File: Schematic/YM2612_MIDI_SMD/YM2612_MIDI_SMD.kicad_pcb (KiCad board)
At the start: 2 copper layers, 100 x 100 mm, 125 parts, among them J1 Barrel_Jack_12V, J2 USB_B, J3 DIN-5_180, J4 Audio-Jack-3, J5 Micro_SD_Card, J6 ICSP, SW1 SW_Push_Dual, SW10 SW_Push_Dual, SW2 SW_Push_Dual, SW3 SW_Push_Dual, SW4 SW_Push_Dual, SW5 SW_Push_Dual, SW6 SW_Push_Dual, SW7 SW_Push_Dual, SW8 SW_Push_Dual, SW9 Rotary_Encoder_Switch, U1 LM2596S-5, U10 LD1117S33TR_SOT223, U11 4050, U2 AT90USB1286-AU, U3 YM2612, U4 SN76489, U6 H11L1, U8 TPA3122D2, U9 TL062, Y1 16MHz

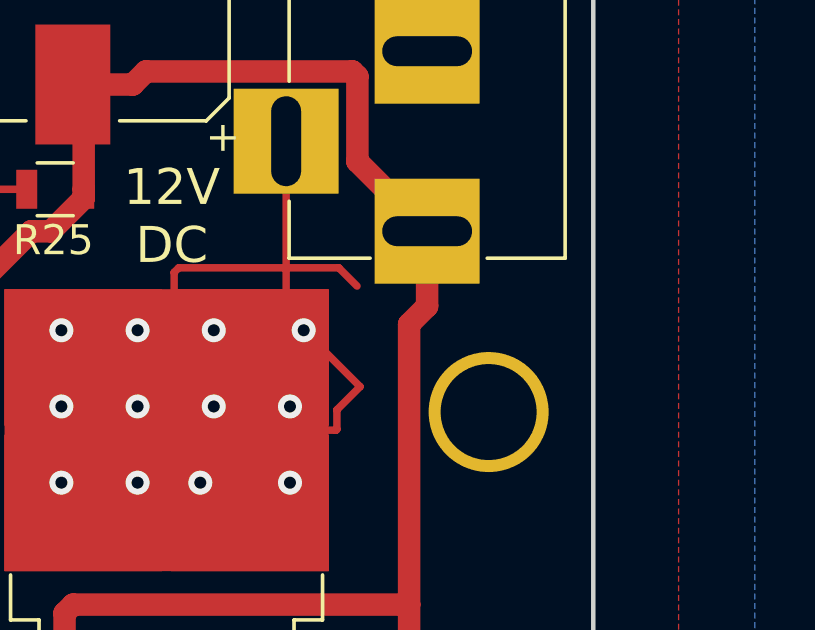
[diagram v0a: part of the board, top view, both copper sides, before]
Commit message: Added center-positive logo to FSS
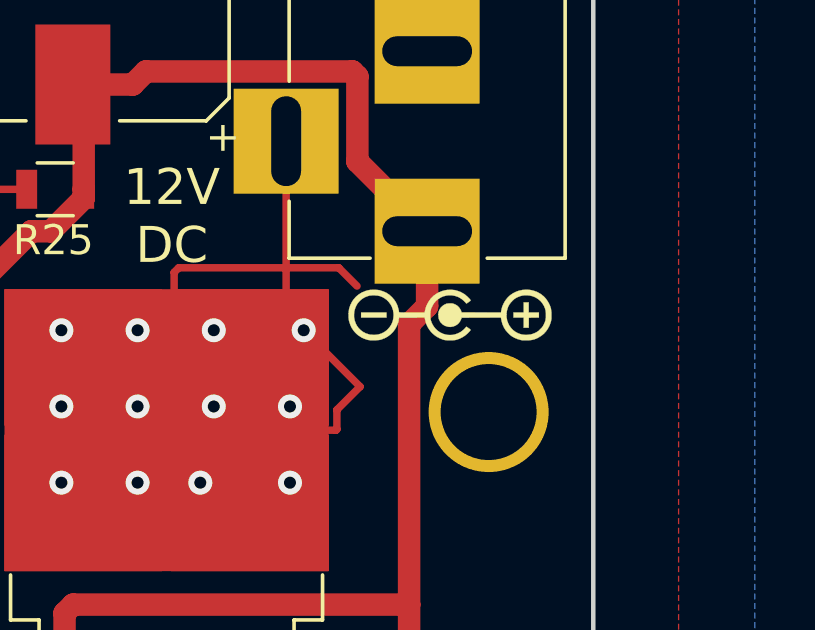
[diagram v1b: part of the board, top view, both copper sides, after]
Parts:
- added G***: LOGO, art:Center_Positive_Logo, F.Cu at (268.2, 63.0)

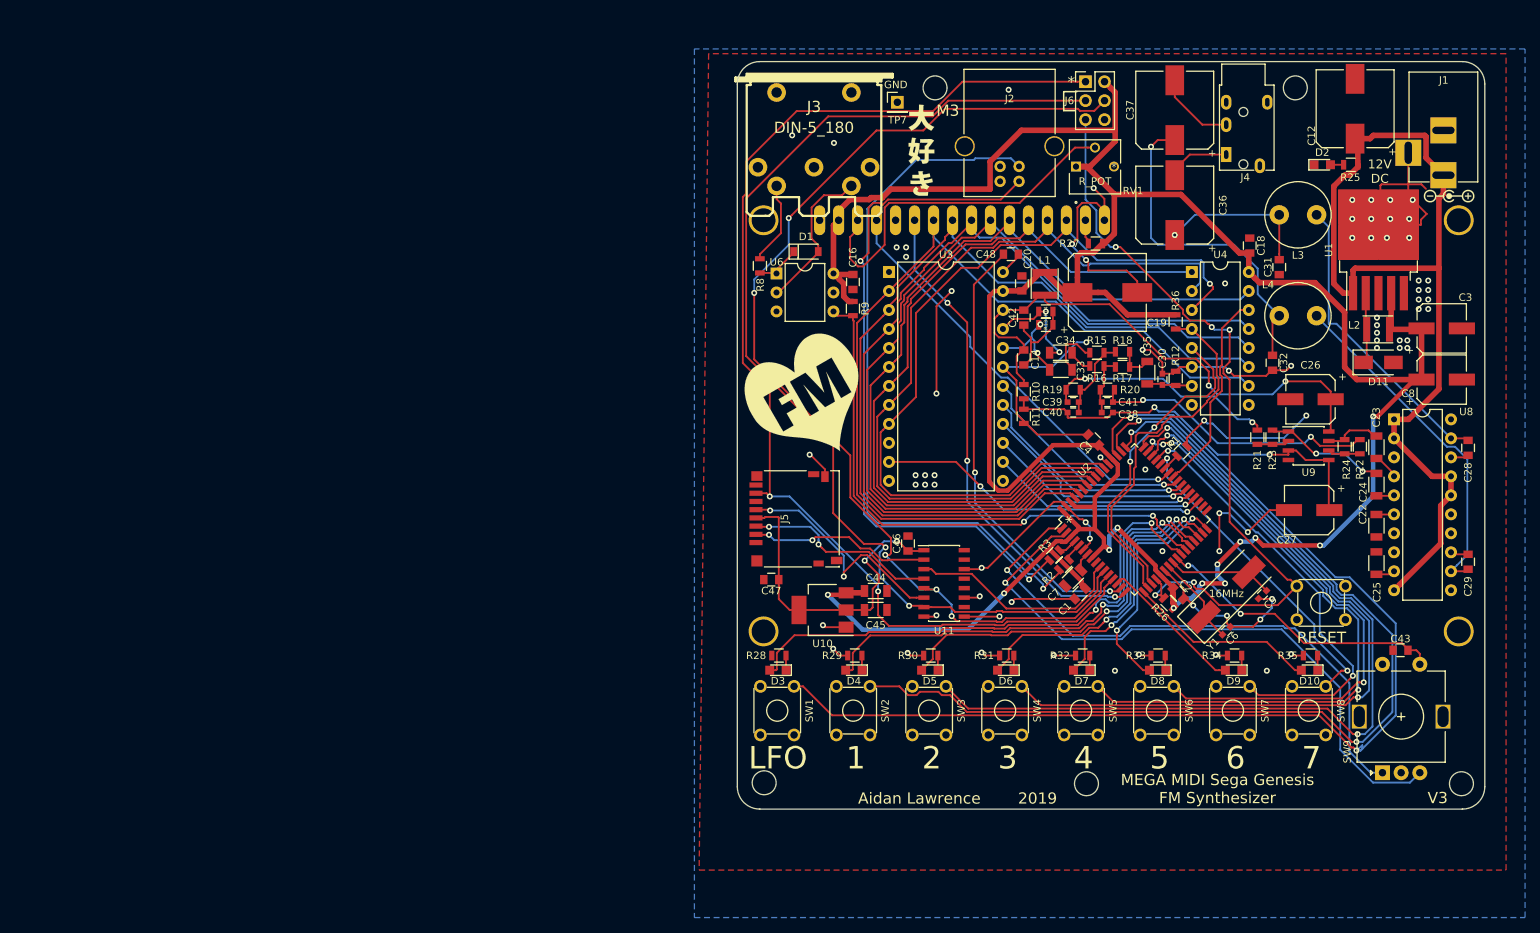
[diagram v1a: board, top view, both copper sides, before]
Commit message: Fixed minor bug on favorite button #7
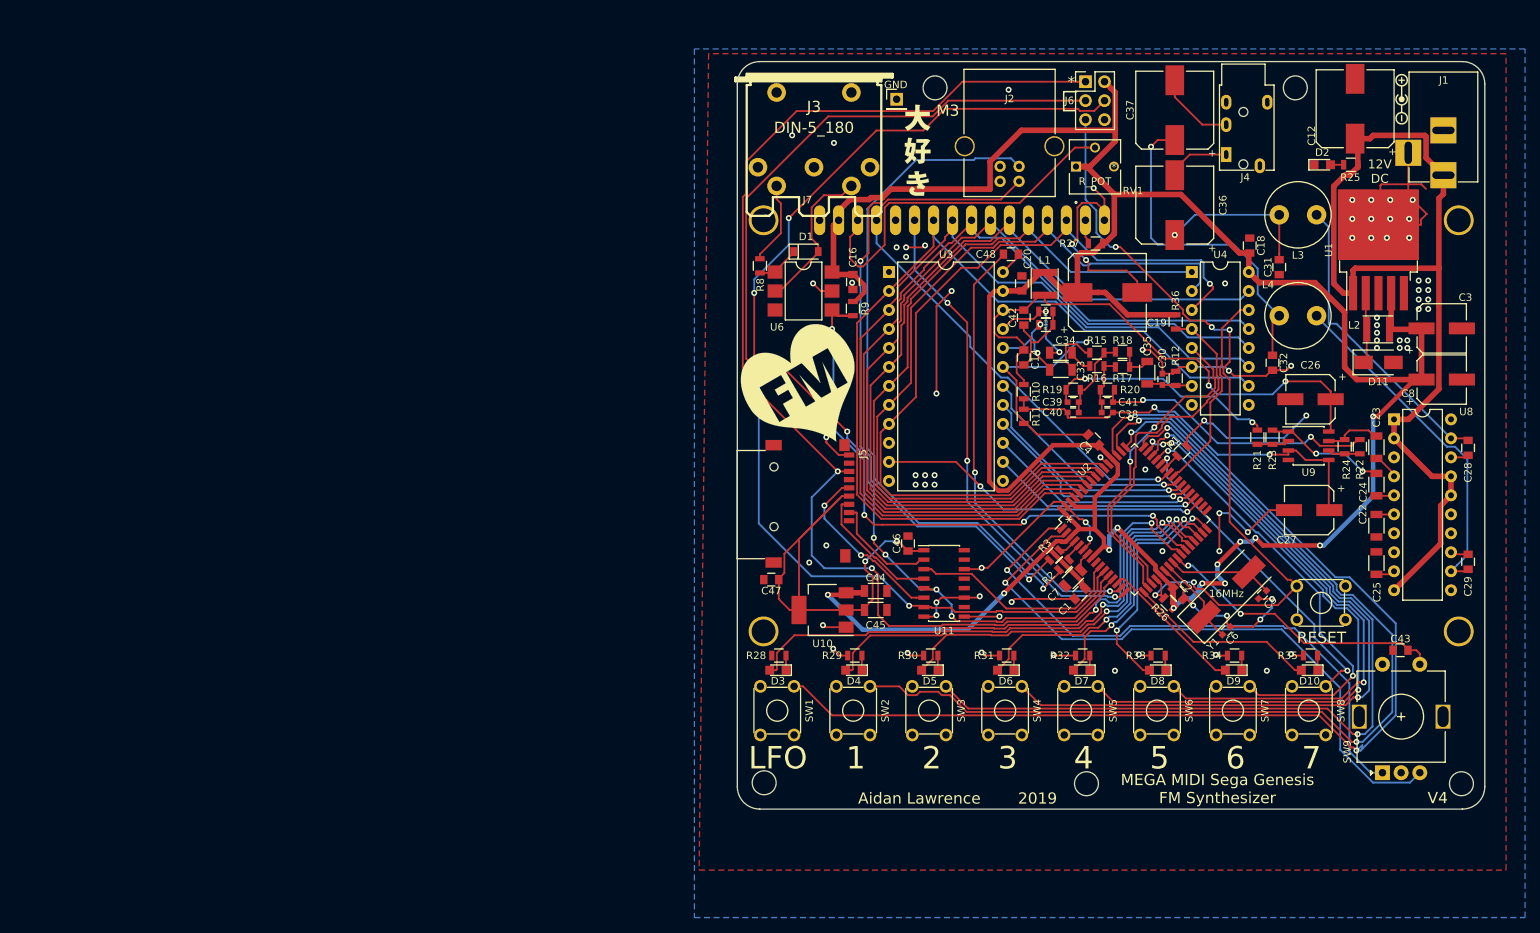
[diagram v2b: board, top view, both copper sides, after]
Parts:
- removed TP7: TP_GND, Pin_Headers:Pin_Header_Straight_1x01_Pitch2.54mm
- added J7: TP_GND, Pin_Headers:Pin_Header_Straight_1x01_Pitch2.54mm, F.Cu at (194.3, 50.0)
- J5: footprint Connector_Card:microSD_HC_Hirose_DM3D-SF -> customMicroSD:SOFNG_TF_15x15_PUSH_PUSH
- U6: footprint Housings_DIP:DIP-6_W7.62mm -> Housings_DIP:SMDIP-6_W7.62mm
- moved G*** 14.4 mm to (261.9, 50.0), turned to 90 degrees
- moved J5 7.12 mm to (188.0, 106.4), turned to 90 degrees
- moved U6 4.32 mm to (181.9, 75.7)
- moved G*** 1.37 mm to (182.4, 89.2)
- moved G*** 0.51 mm to (197.1, 56.9)
- moved G*** 0.25 mm to (223.0, 93.7)
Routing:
- net +3V3: track 44.3 -> 64.9 mm
- net GND: track 270.5 -> 283.3 mm, vias 81 -> 87
- net Net-(J5-Pad2): track 24.3 -> 14.7 mm, vias 2 -> 0
- net Net-(J5-Pad3): track 26.1 -> 17.7 mm, vias 2 -> 0
- net Net-(J5-Pad5): track 31.7 -> 23.7 mm
- net MIDI_IN: track 75.8 -> 81.5 mm, vias 2 -> 4
- net MISO: track 156.9 -> 161.4 mm
- net USB_D+: track 96.1 -> 92.9 mm
- net USB_D-: track 92.9 -> 89.7 mm
- net SCK: track 147.2 -> 150.4 mm
- net MOSI: track 143.8 -> 144.4 mm, vias 5 -> 7
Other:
- board text added: "V4"
- board text removed: "V3"

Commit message: Analog stage
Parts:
- removed C33, C34, C44, C45: 10uF, Capacitors_SMD:C_1206
- removed C35: 1uF, Capacitors_SMD:C_1206
- removed C36, C37: 1000uF, Capacitors_SMD:CP_Elec_10x10
- removed C38, C39, C40, C41: 5.6nF, Capacitors_SMD:C_0603
- removed C42, C43, C46, C47, C48: 100nF, Capacitors_SMD:C_0805
- removed D3: LED_Small, LEDs:LED_0805
- removed G***: LOGO, art:logo_3
- removed G***: LOGO, art:logo_2
- removed G***: LOGO, art:Center_Positive_Logo
- removed G***: LOGO, art:logo_1
- removed J4: Audio-Jack-3, Connectors:PJ320E_3.5mm_Jack
- removed L2: 33uH, custom_inductors:L_4x4
- removed L3, L4: 2.2mH, Inductors_THT:L_Radial_D8.7mm_P5.00mm_Fastron_07HCP
- removed R31, R32, R33, R34, R35: 220, Resistors_SMD:R_0805
- removed R36: 2.2k, Resistors_SMD:R_0805
- removed U11: 4050, Housings_SOIC:SOIC-16_3.9x9.9mm_Pitch1.27mm
- added C10: 100nF, Capacitors_SMD:C_0805, F.Cu at (136.2, 111.7)
- added C11: 100nF, Capacitors_SMD:C_0805, F.Cu at (128.5, 118.0)
- added C13: 10uF, Capacitors_SMD:C_1206, F.Cu at (92.7, 123.6)
- added C15: 10uF, Capacitors_SMD:C_1206, F.Cu at (93.6, 102.8)
- added C17: 10uF, Capacitors_SMD:C_1206, F.Cu at (222.3, 80.7)
- added C21: 1uF, Capacitors_SMD:C_0805, F.Cu at (261.1, 98.0)
- added C9: 10uF, Capacitors_SMD:C_1206, F.Cu at (206.7, 90.8)
- added R4: 22, Resistors_SMD:R_0805, F.Cu at (163.6, 92.3)
- added R5: 22, Resistors_SMD:R_0805, F.Cu at (160.1, 94.1)
- added R6: 220, Resistors_SMD:R_0805, F.Cu at (154.5, 99.6)
- added R7: 270, Resistors_SMD:R_0805, F.Cu at (163.6, 90.4)
- added U5: SD6271LR, TO_SOT_Packages_SMD:SOT-23-6, F.Cu at (210.9, 76.3)
- added U7: 4050, Housings_SOIC:SOIC-16_3.9x9.9mm_Pitch1.27mm, F.Cu at (232.6, 65.6)
- C12: value 1000uF -> 100nF; footprint Capacitors_SMD:CP_Elec_10x10 -> Capacitors_SMD:C_0805
- C16: value 100nF -> 10uF; footprint Capacitors_SMD:C_0805 -> Capacitors_SMD:C_1206
- C18: value 100nF -> 100uF; footprint Capacitors_SMD:C_0805 -> Capacitors_SMD:CP_Elec_6.3x7.7
- C19: value 1000uF -> 10uF; footprint Capacitors_SMD:CP_Elec_10x10 -> Capacitors_SMD:C_1206
- C20: value 100nF -> 1uF
- C22, C23: value 1uF -> 10uF
- C24, C25: value 1uF -> 270pF; footprint Capacitors_SMD:C_1206 -> Capacitors_SMD:C_0805
- C26: value 68uF -> 100nF; footprint Capacitors_SMD:CP_Elec_6.3x5.8 -> Capacitors_SMD:C_0805
- C27, C3, C8: value 100uF -> 100nF; footprint Capacitors_SMD:CP_Elec_6.3x7.7 -> Capacitors_SMD:C_0805
- C28: value 0.22uF -> 100nF
- C29: value 0.22uF -> 100uF; footprint Capacitors_SMD:C_0805 -> Capacitors_SMD:CP_Elec_6.3x7.7
- C30: value 220pF -> 100uF; footprint Capacitors_SMD:C_0603 -> Capacitors_SMD:CP_Elec_6.3x7.7
- C31, C32: value 68nF -> 10uF; footprint Capacitors_SMD:C_0805 -> Capacitors_SMD:C_1206
- C4: value 100nF -> 22pF; footprint Capacitors_SMD:C_0805 -> Capacitors_SMD:C_0603
- C6: value 22pF -> 1uF; footprint Capacitors_SMD:C_0603 -> Capacitors_SMD:C_1206
- C7: value 1uF -> 100nF; footprint Capacitors_SMD:C_1206 -> Capacitors_SMD:C_0805
- D11: value SS34_SMA -> LED_Small; footprint Diodes_SMD:D_SMA -> LEDs:LED_0805
- D2: value LED_Small -> SS34; footprint LEDs:LED_0805 -> Diodes_SMD:D_SMA
- J1: value Barrel_Jack_12V -> DIN-5_180; footprint Connectors:BARREL_JACK -> midicon:din-5
- J2: value USB_B -> TP_GND; footprint Connectors:USB_B -> Pin_Headers:Pin_Header_Straight_1x01_Pitch2.54mm
- J3: value DIN-5_180 -> USB_B; footprint midicon:din-5 -> Connectors:USB_B
- J5: value Micro_SD_Card -> ICSP; footprint customMicroSD:SOFNG_TF_15x15_PUSH_PUSH -> Pin_Headers:Pin_Header_Straight_2x03_Pitch2.54mm
- J6: value ICSP -> Audio-Jack-3; footprint Pin_Headers:Pin_Header_Straight_2x03_Pitch2.54mm -> Boom Precision Elec PJ-307C:SWITCHCRAFT_35RAPC4BHN2
- J7: value TP_GND -> Micro_SD_Card; footprint Pin_Headers:Pin_Header_Straight_1x01_Pitch2.54mm -> customMicroSD:SOFNG_TF_15x15_PUSH_PUSH
- L1: value 33uH -> 4.7uH
- R1: value 1k -> 10k
- R10, R11: value 47k -> 220
- R12, R13, R14, R15, R16: value 2.2k -> 220
- R17: value 33k -> 220
- R18: value 33k -> 10K
- R19: value 10k -> 10K
- R2: value 22 -> 220
- R20, R21, R22: value 10k -> 2.2K
- R23: value 33k -> 6.2K
- R24: value 33k -> 51K
- R25: value 1k -> 51K
- R26: value 10k -> 6.2K
- R27, R28: value 220 -> 160K
- R29: value 220 -> 10K
- R3: value 22 -> 1k
- R30: value 220 -> 1K
- R8: value 220 -> 51K
- R9: value 270 -> 2.2k
- SW1: value SW_Push_Dual -> Rotary_Encoder_Switch; footprint Buttons_Switches_THT:SW_TH_Tactile_Omron_B3F-10xx -> Rotary_Encoder:RotaryEncoder_Alps_EC11E-Switch_Vertical_H20mm
- SW9: value Rotary_Encoder_Switch -> SW_Push_Dual; footprint Rotary_Encoder:RotaryEncoder_Alps_EC11E-Switch_Vertical_H20mm -> Buttons_Switches_THT:SW_TH_Tactile_Omron_B3F-10xx
- U1: value LM2596S-5 -> H11L1; footprint TO_SOT_Packages_SMD:TO-263-5_TabPin3 -> Housings_DIP:SMDIP-6_W7.62mm
- U10: value LD1117S33TR_SOT223 -> LD1117S50TR_SOT223
- U6: value H11L1 -> LD1117S33TR_SOT223; footprint Housings_DIP:SMDIP-6_W7.62mm -> TO_SOT_Packages_SMD:SOT-223-3_TabPin2
- U8: value TPA3122D2 -> TL072; footprint Housings_DIP:DIP-20_W7.62mm -> Housings_SOIC:SOIC-8_3.9x4.9mm_Pitch1.27mm
- U9: value TL062 -> LD1117S50TR_SOT223; footprint Housings_SOIC:SOIC-8_3.9x4.9mm_Pitch1.27mm -> TO_SOT_Packages_SMD:SOT-223-3_TabPin2
- moved C5 163.2 mm to (80.5, 127.3), turned to 0 degrees
- moved C6 155.5 mm to (83.0, 125.5), turned to 0 degrees
- moved C8 152.5 mm to (119.7, 126.3)
- moved C12 149.4 mm to (124.6, 123.0), turned to 0 degrees
- moved C4 146.5 mm to (77.6, 127.3), turned to 0 degrees
- moved Y1 141.3 mm to (97.3, 109.4), turned to 0 degrees
- moved R1 139.5 mm to (96.0, 125.7), turned to 0 degrees
- moved C31 139.2 mm to (110.9, 107.8), turned to 0 degrees
- moved SW9 127.1 mm to (146.0, 82.4), turned to 0 degrees
- moved SW8 126.2 mm to (126.7, 111.5), turned to 0 degrees
- moved SW10 123.1 mm to (125.2, 104.7)
- moved D9 114.7 mm to (124.8, 121.2), turned to 0 degrees
- moved C28 114.0 mm to (156.8, 93.9), turned to 0 degrees
- moved D10 108.9 mm to (143.7, 101.0), turned to 0 degrees
- moved C3 106.8 mm to (160.7, 88.5)
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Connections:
- C12 pad 1: +12V -> GND
- C12 pad 2: GND -> +5V
- C14 pad 2: AVCC -> +5VA
- C16 pad 1: +5V -> GND
- C16 pad 2: GND -> Net-(C13-Pad2)
- C18 pad 1: +5V -> +2V5
- C19 pad 1: +5V -> Net-(C19-Pad1)
- C19 pad 2: GND -> MOL
- C20 pad 1: GND -> Net-(C20-Pad1)
- C20 pad 2: +5V -> PSG_OUT
- C22 pad 2: GND -> MOR
- C23 pad 1: PRE_L -> GND
- C23 pad 2: Net-(C23-Pad2) -> Net-(C13-Pad2)
- C24 pad 1: PRE_R -> Net-(C24-Pad1)
- C25 pad 2: GND -> Net-(C25-Pad2)
- C26 pad 1: AVCC -> +3V3
- C27 pad 1: AVCC_DIV2 -> +5VA
- C28 pad 1: Net-(C28-Pad1) -> +3V3
- C28 pad 2: Net-(C28-Pad2) -> GND
- C29 pad 1: Net-(C29-Pad1) -> Net-(C24-Pad1)
- C29 pad 2: Net-(C29-Pad2) -> L_OUT
- C30 pad 1: PSG_OUT -> Net-(C25-Pad1)
- C30 pad 2: GND -> R_OUT
- C31 pad 2: Net-(C31-Pad2) -> +5VA
- C32 pad 1: Net-(C32-Pad1) -> GND
- C32 pad 2: GND -> +5V
- C4 pad 1: +5V -> Net-(C4-Pad1)
- C7 pad 1: Net-(C7-Pad1) -> +5V
- C8 pad 1: +5V -> RE_SW
- D10 pad 2: LED_8 -> LED_7
- D11 pad 2: GND -> LED_8
- D2 pad 1: GND -> Net-(C13-Pad2)
- D4 pad 2: LED_2 -> LED_1
- D5 pad 2: LED_3 -> LED_2
- D6 pad 2: LED_4 -> LED_3
- D7 pad 2: LED_5 -> LED_4
- D8 pad 2: LED_6 -> LED_5
- D9 pad 2: LED_7 -> LED_6
- J1 pad 1: +12V -> Net-(J1-Pad1)
- J1 pad 2: GND -> Net-(J1-Pad2)
- J1 pad 3: GND -> Net-(J1-Pad3)
- J2 pad 1: Net-(J2-Pad1) -> GND
- J3 pad 1: Net-(J3-Pad1) -> VBUS
- J3 pad 2: Net-(J3-Pad2) -> USB_D-
- J3 pad 3: Net-(J3-Pad3) -> USB_D+
- J3 pad 4: Net-(J3-Pad4) -> GND
- J3 pad 5: Net-(D1-Pad2) -> GND
- J5 pad 1: Net-(J5-Pad1) -> MISO
- J5 pad 2: Net-(J5-Pad2) -> +5V
- J5 pad 3: Net-(J5-Pad3) -> SCK
- J5 pad 4: +3V3 -> MOSI
- J5 pad 5: Net-(J5-Pad5) -> RESET
- J6 pad 1: MISO -> L_OUT
- J6 pad 2: +5V -> R_OUT
- J6 pad 3: SCK -> GND
- J7 pad 1: GND -> Net-(J7-Pad1)
- L1 pad 1: +5V -> Net-(D2-Pad2)
- L1 pad 2: AVCC -> VBUS
- R1 pad 1: Net-(R1-Pad1) -> +5V
- R1 pad 2: GND -> RESET
- R10 pad 1: AVCC -> Net-(D4-Pad1)
- R10 pad 2: AVCC_DIV2 -> GND
- R11 pad 1: AVCC_DIV2 -> Net-(D5-Pad1)
- R12 pad 1: PSG_OUT -> Net-(D6-Pad1)
- R13 pad 1: MOR -> Net-(D7-Pad1)
- R14 pad 1: MOL -> Net-(D8-Pad1)
- R15 pad 1: Net-(C38-Pad2) -> Net-(D9-Pad1)
- R15 pad 2: Net-(C33-Pad1) -> GND
- R16 pad 1: Net-(C40-Pad2) -> Net-(D10-Pad1)
- R16 pad 2: Net-(C34-Pad1) -> GND
- R17 pad 1: Net-(C40-Pad2) -> Net-(D11-Pad1)
- R17 pad 2: Net-(C35-Pad1) -> GND
- R18 pad 1: Net-(C38-Pad2) -> +5VA
- R18 pad 2: Net-(C35-Pad1) -> +2V5
- R19 pad 1: Net-(C39-Pad1) -> +2V5
- R19 pad 2: Net-(C38-Pad2) -> GND
- R2 pad 1: Net-(R2-Pad1) -> Net-(D1-Pad1)
- R2 pad 2: USB_D+ -> Net-(J1-Pad4)
- R20 pad 1: Net-(C41-Pad1) -> MOL
- R20 pad 2: Net-(C40-Pad2) -> GND
- R21 pad 1: Net-(R21-Pad1) -> PSG_OUT
- R21 pad 2: Net-(C39-Pad1) -> GND
- R22 pad 1: Net-(R22-Pad1) -> MOR
- R22 pad 2: Net-(C41-Pad1) -> GND
- R23 pad 1: PRE_R -> Net-(C24-Pad2)
- R23 pad 2: Net-(R21-Pad1) -> Net-(C19-Pad1)
- R24 pad 1: PRE_L -> Net-(C24-Pad2)
- R24 pad 2: Net-(R22-Pad1) -> Net-(C20-Pad1)
- R25 pad 1: +12V -> Net-(C25-Pad2)
- R25 pad 2: Net-(D2-Pad2) -> Net-(C21-Pad1)
- R26 pad 1: +5V -> Net-(C25-Pad2)
- R26 pad 2: RESET -> Net-(C22-Pad1)
- R27 pad 1: +5V -> Net-(C24-Pad1)
- R27 pad 2: Net-(DS1-Pad15) -> Net-(C24-Pad2)
- R28 pad 1: Net-(D3-Pad1) -> Net-(C25-Pad1)
- R28 pad 2: GND -> Net-(C25-Pad2)
- R29 pad 1: Net-(D4-Pad1) -> Net-(C13-Pad2)
- R29 pad 2: GND -> Net-(R29-Pad2)
- R3 pad 2: USB_D- -> GND
- R30 pad 1: Net-(D5-Pad1) -> Net-(R29-Pad2)
- R8 pad 1: Net-(D1-Pad1) -> Net-(R8-Pad1)
- R8 pad 2: Net-(J3-Pad4) -> GND
- R9 pad 2: MIDI_IN -> PSG_RDY
- SW10 pad 1: RESET -> B8
- SW2 pad 1: B2 -> B1
- SW3 pad 1: B3 -> B5
- SW4 pad 1: B4 -> B2
- SW5 pad 1: B5 -> B6
- SW6 pad 1: B6 -> B3
- SW8 pad 1: B8 -> RESET
- U1 pad 1: +12V -> Net-(D1-Pad1)
- U1 pad 2: Net-(D11-Pad1) -> Net-(D1-Pad2)
- U1 pad 3: GND -> Net-(U1-Pad3)
- U1 pad 4: +5V -> MIDI_IN
- U10 pad 2: +3V3 -> +5V
- U10 pad 3: +5V -> Net-(C13-Pad2)
- U2 pad 23: Net-(C6-Pad1) -> Net-(C5-Pad1)
- U2 pad 24: Net-(C5-Pad1) -> Net-(C4-Pad1)
- U2 pad 4: Net-(R3-Pad1) -> Net-(R5-Pad1)
- U2 pad 43: Net-(R1-Pad1) -> Net-(R3-Pad1)
- U2 pad 5: Net-(R2-Pad1) -> Net-(R4-Pad1)
- U2 pad 7: Net-(C7-Pad1) -> Net-(C6-Pad1)
- U3 pad 22: AVCC -> +5VA
- U4 pad 16: +5V -> +5VA
- U6 pad 1: Net-(D1-Pad1) -> GND
- U6 pad 2: Net-(D1-Pad2) -> +3V3
- U6 pad 3: Net-(U6-Pad3) -> Net-(C13-Pad2)
- U8 pad 1: +12V -> Net-(C24-Pad1)
- U8 pad 2: +12V -> Net-(C24-Pad2)
- U8 pad 3: GND -> +2V5
- U8 pad 4: Net-(C23-Pad2) -> GND
- U8 pad 5: Net-(C24-Pad2) -> +2V5
- U8 pad 6: Net-(C22-Pad1) -> Net-(C25-Pad2)
- U8 pad 7: GND -> Net-(C25-Pad1)
- U8 pad 8: GND -> +5VA
- U9 pad 1: PRE_R -> GND
- U9 pad 2: Net-(R21-Pad1) -> +5VA
- U9 pad 3: AVCC_DIV2 -> Net-(C13-Pad2)
- Y1 pad 1: Net-(C6-Pad1) -> Net-(C5-Pad1)
- Y1 pad 2: Net-(C5-Pad1) -> Net-(C4-Pad1)
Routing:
- net +5V: track 398.6 -> 0.00 mm, vias 12 -> 0
- net GND: track 283.3 -> 0.00 mm, vias 87 -> 65
- net MISO: track 161.4 -> 0.00 mm, vias 2 -> 0
- net B1: track 154.1 -> 0.00 mm, vias 2 -> 0
- net SCK: track 150.4 -> 0.00 mm, vias 2 -> 0
- net MOSI: track 144.4 -> 0.00 mm, vias 7 -> 0
- net B2: track 138.0 -> 0.00 mm, vias 2 -> 0
- net D0: track 125.8 -> 0.00 mm
- net D1: track 122.9 -> 0.00 mm
- net +12V: track 122.1 -> 0.00 mm
- net B3: track 121.0 -> 0.00 mm, vias 2 -> 0
- net D2: track 119.7 -> 0.00 mm
- net D3: track 117.0 -> 0.00 mm
- net D4: track 115.7 -> 0.00 mm
- net D7: track 112.9 -> 0.00 mm, vias 1 -> 0
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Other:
- board text added: "V5"
- board text removed: "*"
- board text removed: "12V DC"
- board text removed: "12V DC Center-Positive"
- board text removed: "16MHz"
- board text removed: "GND"
- board text removed: "M3"
- board text removed: "RESET"
- board text removed: "V4"

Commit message: Route complete
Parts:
- moved C15 158.5 mm to (247.4, 64.5)
- moved SW1 156.0 mm to (258.7, 140.5), turned to 90 degrees
- moved C31 143.8 mm to (247.4, 62.5)
- moved R1 143.2 mm to (217.6, 50.0), turned to 270 degrees
- moved C8 141.4 mm to (261.1, 122.9), turned to 180 degrees
- moved C11 139.9 mm to (268.0, 106.7), turned to 180 degrees
- moved C12 131.7 mm to (242.8, 65.0)
- moved C6 129.2 mm to (208.3, 93.7), turned to 135 degrees
- moved C4 129.1 mm to (206.5, 119.1), turned to 135 degrees
- moved C13 126.8 mm to (212.3, 81.5)
- moved SW10 126.0 mm to (247.7, 134.6), turned to 90 degrees
- moved C5 122.1 mm to (201.9, 114.6), turned to 315 degrees
- moved C14 115.4 mm to (259.6, 69.8), turned to 180 degrees
- moved SW5 113.2 mm to (227.3, 134.6), turned to 90 degrees
- moved Y1 109.6 mm to (206.8, 114.6), turned to 315 degrees
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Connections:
- net Net-(C13-Pad2) renamed 6.6VBOOST
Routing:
- net +5V: track 0.00 -> 251.5 mm
- net B1: track 0.00 -> 119.5 mm, vias 0 -> 2
- net RE_B: track 0.00 -> 116.3 mm, vias 0 -> 3
- net RE_A: track 0.00 -> 115.9 mm, vias 0 -> 3
- net D5: track 0.00 -> 111.3 mm, vias 0 -> 1
- net D4: track 0.00 -> 109.4 mm, vias 0 -> 1
- net RESET: track 0.00 -> 107.4 mm, vias 0 -> 6
- net B2: track 0.00 -> 107.4 mm, vias 0 -> 3
- net D2: track 0.00 -> 107.0 mm, vias 0 -> 1
- net D1: track 0.00 -> 106.8 mm, vias 0 -> 1
- net D3: track 0.00 -> 106.5 mm, vias 0 -> 1
- net GND: track 0.00 -> 106.1 mm, vias 65 -> 164
- net D0: track 0.00 -> 106.1 mm, vias 0 -> 1
- net D6: track 0.00 -> 105.3 mm, vias 0 -> 1
- net D7: track 0.00 -> 103.8 mm, vias 0 -> 1
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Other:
- board text added: "*"

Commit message: Silk screen
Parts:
- added G***: LOGO, art:logo_1, B.Cu at (223.0, 93.5)
- added G***: LOGO, art:logo_2, F.Cu at (182.6, 94.2)
- added G***: LOGO, art:logo_3, F.Cu at (199.4, 56.9)
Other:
- board text added: "3.3V"
- board text added: "5V"
- board text added: "RESET"

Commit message: PCB Complete
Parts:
- RV1: value R_POT -> LCD CONT
- moved C31 1.52 mm to (247.4, 61.0)
- moved J5 0.41 mm to (220.2, 47.7)
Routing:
- net +3V3: track 48.2 -> 35.8 mm, vias 0 -> 2
- net 6.6VBOOST: track 75.0 -> 72.2 mm
- net +5VA: track 111.2 -> 112.7 mm
- net MISO: track 83.5 -> 84.6 mm
- net +5V: track 251.5 -> 251.0 mm
- net GND: vias 164 -> 218
